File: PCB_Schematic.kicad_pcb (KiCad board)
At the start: 2 copper layers, 78.9 x 67.8 mm, 109 parts, among them J1 Conn_01x02_Pin, J2 Programming Header, J3 Ultrasonic, J4 Power_Connector, J5 USB_A, J6 IMU_1, J7 IMU_2, Q1 BSS138, SW1 Reset Switch, U1 STM32F091RCTx, U2 FT232RL, U3 LM1117MP-ADJ, U4 TPS54331-Q1, U5 MAX7375AXR805

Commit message: PCB changes
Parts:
- D10, D7, R10, R11, R13, R8, R9: moved to B.Cu
- D16: moved to F.Cu
- moved C4 154.3 mm to (172.4, 44.2)
- moved R12 151.8 mm to (165.1, 47.8), turned to 180 degrees
- moved C5 147.2 mm to (165.1, 51.3), turned to 180 degrees
- moved R13 145.6 mm to (159.0, 48.2), turned to -90 degrees
- moved TP1 142.4 mm to (169.4, 54.1)
- moved D11 136.7 mm to (169.4, 48.8), turned to 90 degrees
- moved U3 132.1 mm to (166.4, 38.1)
- moved R3 97.2 mm to (137.7, 65.5), turned to 90 degrees
- moved R9 34.9 mm to (138.2, 58.7), turned to 90 degrees
- moved R8 34.1 mm to (142.8, 50.5), turned to 180 degrees
- moved D10 26.6 mm to (141.7, 67.3), turned to 180 degrees
- moved R11 25.5 mm to (146.1, 66.8)
- moved D8 25.4 mm to (140.7, 65.5), turned to 180 degrees
- moved D9 20.1 mm to (146.3, 69.1), turned to 180 degrees
- moved D7 18.6 mm to (147.8, 50.5)
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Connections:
- C1 pad 1: /USB UART Comm/3V3OUT -> /USB UART Comm/VCCIO
- U2 pad 17: /USB UART Comm/3V3OUT -> /USB UART Comm/VCCIO
- U2 pad 4: /USB UART Comm/3V3OUT -> /USB UART Comm/VCCIO
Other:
- board size 78.9 x 67.8 mm -> 78.9 x 74.7 mm

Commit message: layout more
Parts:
- moved J3 181.4 mm to (179.6, 73.4), turned to 90 degrees
- moved J4 175.8 mm to (179.9, 57.5), turned to 90 degrees
- moved Q1 175.7 mm to (171.4, 79.2)
- moved R19 171.8 mm to (178.1, 86.4)
- moved J6 166.4 mm to (155.2, 100.3)
- moved R17 165.1 mm to (173.0, 74.9), turned to -90 degrees
- moved R16 160.8 mm to (165.9, 78.7), turned to 180 degrees
- moved D15 159.1 mm to (172.5, 84.3), turned to 90 degrees
- moved R18 157.7 mm to (167.6, 70.4), turned to -90 degrees
- moved D14 155.3 mm to (172.7, 70.3), turned to -90 degrees
- moved J7 148.0 mm to (138.3, 100.1)
- moved R24 146.3 mm to (152.6, 89.2), turned to 180 degrees
- moved TP2 145.1 mm to (166.1, 83.8)
- moved D3 142.5 mm to (164.6, 90.9)
- moved D4 142.5 mm to (164.6, 94.0)
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
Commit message: PCB
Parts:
- moved D26 176.1 mm to (173.0, 85.0), turned to 90 degrees
- moved R28 171.3 mm to (173.5, 80.0), turned to -90 degrees
- moved R27 170.9 mm to (173.5, 75.4), turned to 180 degrees
- moved D25 170.7 mm to (168.7, 74.9)
- moved D27 161.1 mm to (157.7, 88.9), turned to 180 degrees
- moved R29 153.2 mm to (152.7, 90.2)
- moved R31 145.5 mm to (146.5, 89.9), turned to 180 degrees
- moved D29 143.1 mm to (141.5, 88.7), turned to -90 degrees
- moved R30 133.5 mm to (131.3, 94.5), turned to 180 degrees
- moved D28 130.4 mm to (125.8, 93.2)
- moved D3 129.2 mm to (42.4, 49.0)
- moved D4 129.2 mm to (42.4, 52.1)
- moved D5 129.2 mm to (42.4, 55.1)
- moved D6 129.2 mm to (42.4, 58.1)
- moved R4 129.2 mm to (52.0, 49.8)
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
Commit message: more
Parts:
- moved D4 196.4 mm to (234.7, 92.0)
- moved D5 196.4 mm to (234.7, 95.0)
- moved D6 196.4 mm to (234.7, 98.0)
- moved R5 196.4 mm to (244.3, 92.7)
- moved R6 196.4 mm to (244.3, 95.7)
- moved R7 196.4 mm to (244.3, 98.8)
- moved D3 169.9 mm to (206.2, 94.2)
- moved R4 166.9 mm to (212.6, 95.5)
- moved D1 135.7 mm to (179.6, 39.1), turned to 180 degrees
- moved D2 132.7 mm to (169.7, 59.9)
- moved R2 130.6 mm to (174.3, 59.9)
- moved R1 125.8 mm to (173.5, 39.1), turned to 180 degrees
- moved Cboot1 12.2 mm to (85.0, 36.3)
- moved Ccomp1 12.2 mm to (85.0, 39.4)
- moved Ccomp2 12.2 mm to (89.8, 24.3)
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
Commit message: more
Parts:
- moved H4 179.9 mm to (179.6, 98.0)
- moved H2 160.0 mm to (180.6, 32.0)
- moved H3 130.5 mm to (110.0, 99.1)
- moved H1 94.8 mm to (108.7, 32.8)
- moved Rfbb1 63.4 mm to (138.4, 45.5), turned to 90 degrees
- moved Rcomp1 63.2 mm to (138.4, 40.6), turned to 90 degrees
- moved R14 59.0 mm to (131.8, 50.3)
- moved Rfbt1 58.1 mm to (133.3, 45.5), turned to -90 degrees
- moved L1 50.4 mm to (120.9, 46.0), turned to -90 degrees
- moved Ccomp1 48.9 mm to (133.9, 40.7), turned to 90 degrees
- moved U4 45.4 mm to (127.3, 41.5)
- moved Css1 40.4 mm to (130.0, 36.3), turned to 90 degrees
- moved Cout1 39.9 mm to (126.2, 46.5)
- moved Ccomp2 36.8 mm to (125.0, 35.1)
- moved Cboot1 36.3 mm to (120.9, 41.4), turned to -90 degrees
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
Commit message: more
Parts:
- added C16: .1 uF, Capacitor_SMD:C_0805_2012Metric_Pad1.18x1.45mm_HandSolder, F.Cu at (79.2, 39.0)
- U3: footprint Library:Project_LM1117 -> Package_TO_SOT_SMD:SOT-23-3
- U4: value TPS54331-Q1 -> TPS54331QDRQ1
- moved R7 70.7 mm to (174.2, 89.0)
- moved R5 69.9 mm to (174.5, 96.2)
- moved R6 69.4 mm to (175.0, 93.0)
- moved D6 66.7 mm to (168.6, 89.2), turned to 180 degrees
- moved D4 66.1 mm to (168.8, 96.2), turned to 180 degrees
- moved D5 65.7 mm to (169.0, 93.0), turned to 180 degrees
- moved R4 29.2 mm to (174.2, 99.5)
- moved D3 28.7 mm to (168.7, 99.5), turned to 180 degrees
- moved R14 18.5 mm to (123.0, 34.0), turned to 180 degrees
- moved D13 16.6 mm to (130.8, 34.3), turned to 0 degrees
- moved Ccomp2 16.5 mm to (136.7, 46.8), turned to 90 degrees
- moved Css1 15.3 mm to (117.8, 45.5), turned to 180 degrees
- moved D12 13.1 mm to (127.0, 37.3), turned to 90 degrees
- moved TP3 13.1 mm to (164.5, 34.8)
- moved L1 12.8 mm to (130.8, 37.8), turned to 0 degrees
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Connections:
- Cboot1 pad 1: Net-(U4-BOOT) -> Net-(D12-K)
- Cboot1 pad 2: Net-(D12-K) -> Net-(U4-BOOT)
- U1 pad 14: /DEBUG1 -> unconnected-(U1-PA0-Pad14)
- U1 pad 15: /DEBUG2 -> unconnected-(U1-PA1-Pad15)
- U1 pad 16: /DEBUG3 -> unconnected-(U1-PA2-Pad16)
- U1 pad 17: /DEBUG4 -> unconnected-(U1-PA3-Pad17)
- U1 pad 33: /PB12 -> /DEBUG1
- U1 pad 34: /PB13 -> /DEBUG2
- U1 pad 35: /PB14 -> /DEBUG3
- U1 pad 36: /PB15 -> /DEBUG4
- U4 pad 3: Net-(D12-K) -> unconnected-(U4-EN-Pad3)
- U4 pad 4: GND -> Net-(U4-SS)
- U4 pad 7: unconnected-(U4-EN-Pad7) -> GND
- U4 pad 8: Net-(U4-SS) -> Net-(D12-K)

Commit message: routing v1
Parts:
- added J8: SDOAG_Connector, Library:CONN_B4B-XH-A_JSTProject, F.Cu at (180.3, 40.8)
- J1: footprint Connector_AMASS:AMASS_XT30PW-M_1x02_P2.50mm_Horizontal -> Library:2Pin
- U5: moved to F.Cu
- moved C16 57.2 mm to (136.1, 44.2), turned to 180 degrees
- moved J1 36.6 mm to (111.2, 90.2)
- moved C5 34.6 mm to (131.1, 44.2)
- moved R12 34.5 mm to (131.1, 40.6)
- moved U3 34.5 mm to (132.1, 35.2)
- moved C4 34.5 mm to (139.7, 38.1)
- moved D11 34.5 mm to (135.1, 39.6)
- moved R13 33.9 mm to (127.0, 37.1)
- moved TP1 32.1 mm to (142.3, 41.7)
- moved D1 15.5 mm to (166.6, 50.8)
- moved R1 15.5 mm to (161.1, 50.8)
- moved R3 13.3 mm to (132.1, 62.0)
- moved Cout1 13.2 mm to (124.0, 51.8)
- moved Ccomp1 13.2 mm to (123.9, 55.6)
- moved Cboot1 13.2 mm to (114.8, 48.3)
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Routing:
- net +3.3V: track 0.00 -> 275.6 mm, vias 0 -> 4
- net /SWCLK_IN: track 0.00 -> 154.0 mm
- net /SWDIO_IN: track 0.00 -> 142.0 mm
- net +5V: track 0.00 -> 136.3 mm, vias 0 -> 4
- net /NRST: track 0.00 -> 50.0 mm, vias 0 -> 3
- net /USB UART Comm/VCCIO: track 0.00 -> 41.4 mm, vias 0 -> 2
- net /SDA2: track 0.00 -> 37.0 mm
- net /PC0: track 0.00 -> 36.2 mm
- net /PC1: track 0.00 -> 36.0 mm
- net /Trig: track 0.00 -> 33.8 mm
- net /Echo3.3V: track 0.00 -> 29.9 mm
- net /SCL2: track 0.00 -> 29.8 mm
- net /SDA1: track 0.00 -> 29.5 mm
- net /USBD-: track 0.27 -> 29.5 mm
- net /SCL1: track 0.00 -> 27.4 mm
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
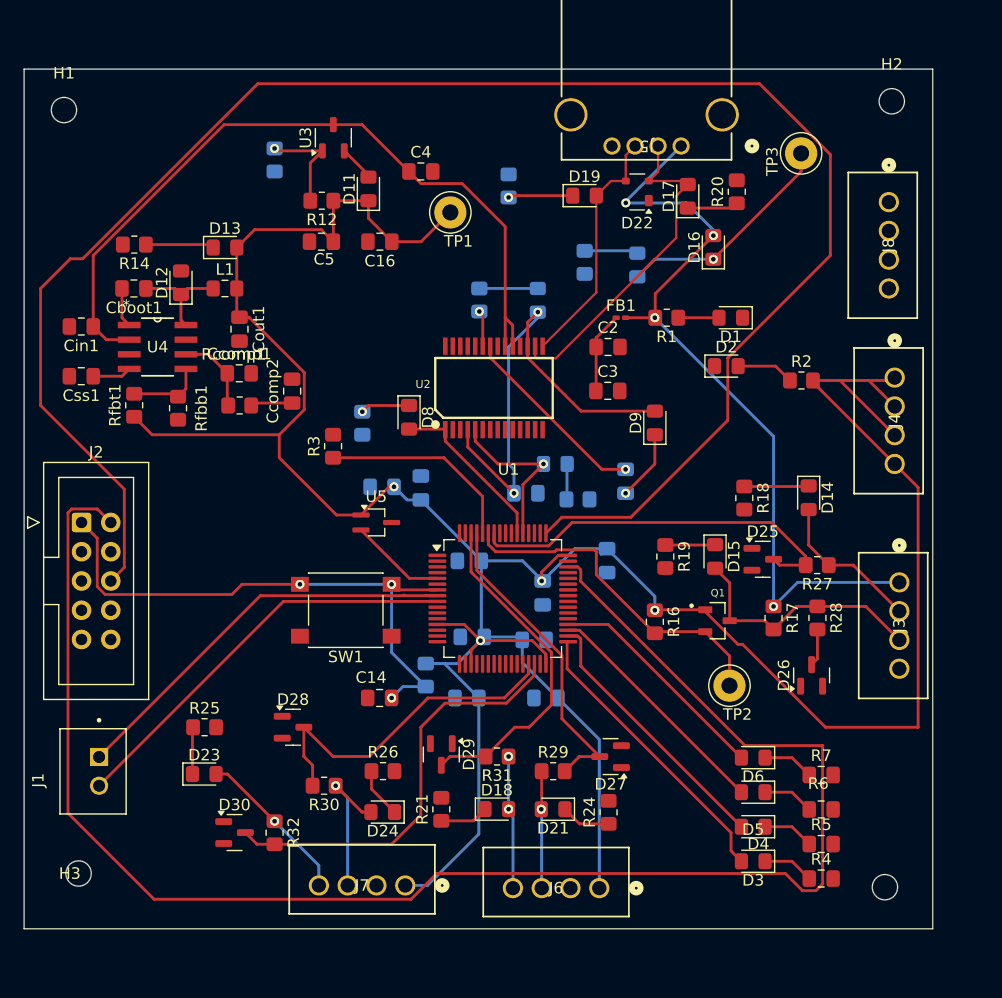
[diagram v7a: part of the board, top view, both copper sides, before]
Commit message: added ground poly and remember you cannot have vias inside pads
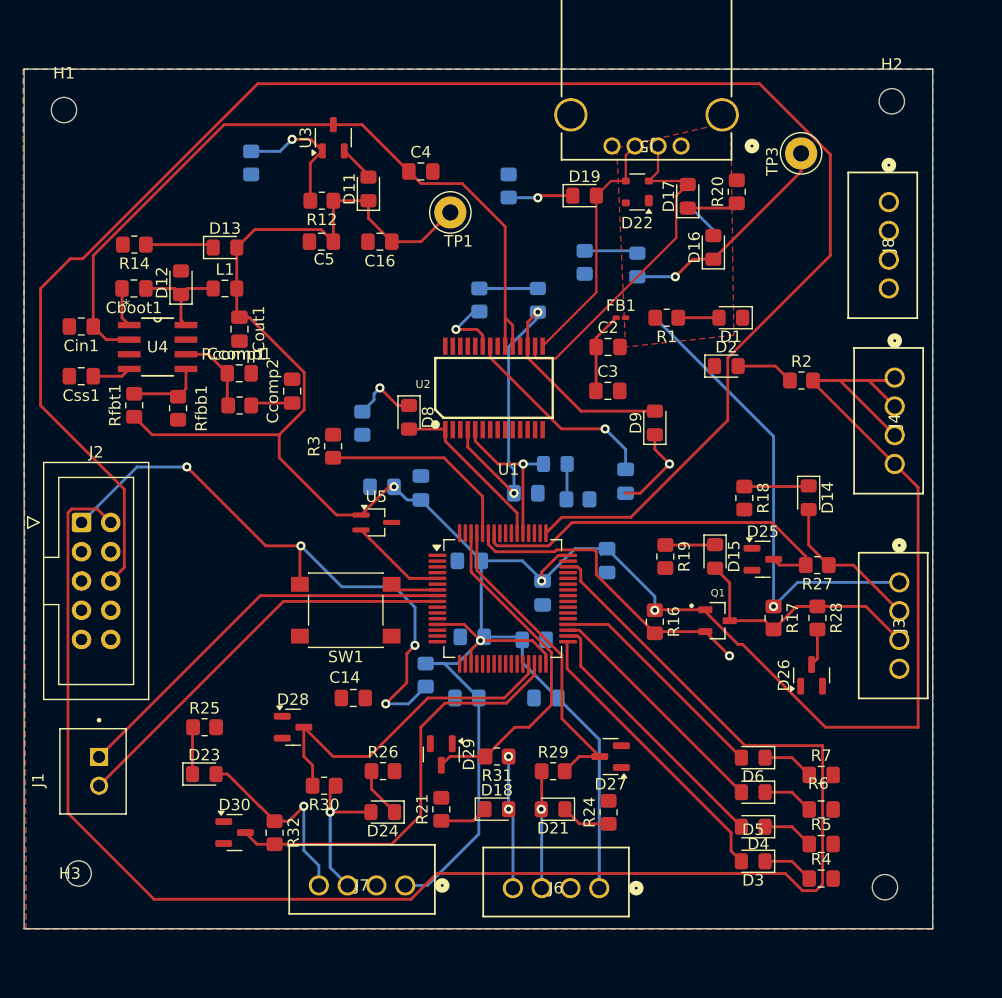
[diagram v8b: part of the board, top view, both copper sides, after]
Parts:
- removed TP2: Echo TP, TestPoint:TestPoint_Loop_D3.50mm_Drill1.4mm_Beaded
- moved C14 2.29 mm to (133.8, 83.8)
- moved R13 2.05 mm to (125.0, 37.4)
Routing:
- net +5V: track 136.3 -> 112.5 mm, vias 4 -> 1
- net /NRST: track 50.0 -> 57.1 mm, vias 3 -> 4
- net Net-(U2-CBUS0): track 3.13 -> 6.16 mm
- net /SDA2E: track 14.7 -> 17.5 mm
- net Net-(U3-ADJ): track 9.00 -> 11.8 mm
- net /Echo3.3V: track 29.9 -> 27.3 mm, vias 0 -> 1
- net Net-(D9-K): track 6.17 -> 7.97 mm
- net Net-(D8-K): track 4.28 -> 5.86 mm
- net /PC0: track 36.2 -> 35.2 mm
- net Net-(U2-CBUS1): track 16.8 -> 17.8 mm
- net /RXD: track 14.5 -> 13.8 mm
- added copper zone on F.Cu, net +5V
- added copper zone on B.Cu, net GND
- added copper zone on F.Cu, net GND
